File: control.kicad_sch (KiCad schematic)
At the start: 28 parts, among them J7 USB_C_Receptacle_USB2.0, J8 Conn_01x04_Male, J9 Conn_ARM_JTAG_SWD_10, U5 AMS1117-3.3, U6 STM32F042C4Tx

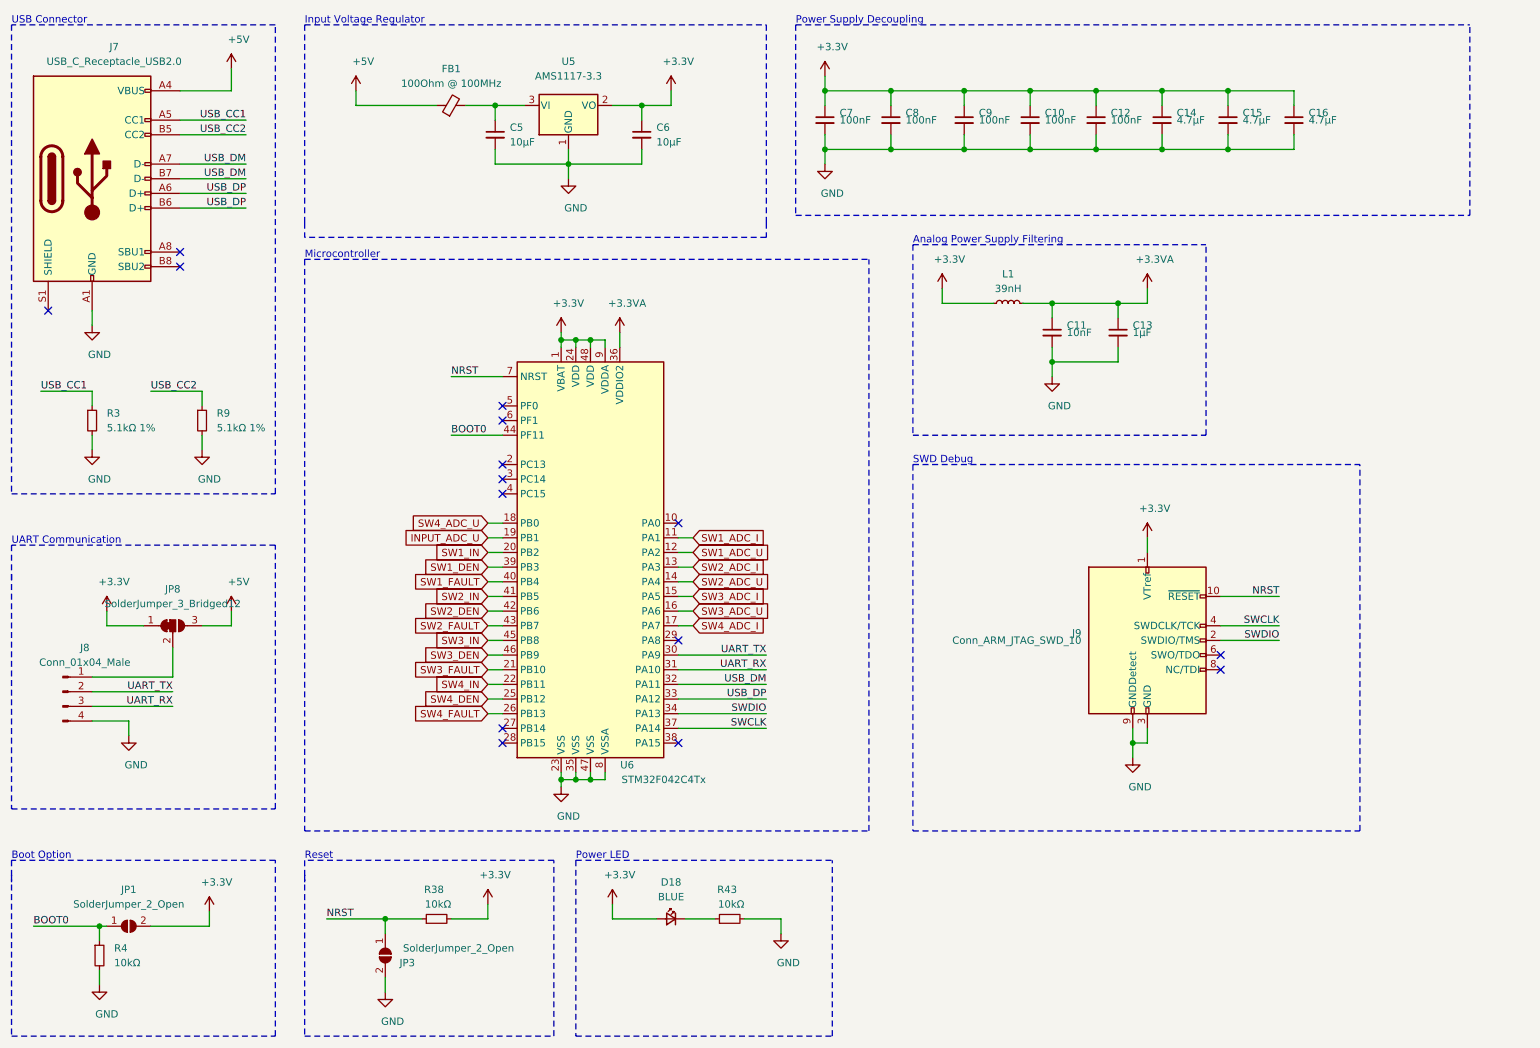
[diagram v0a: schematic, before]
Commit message: place decoupling capacitors nicer, add USB ESD protection
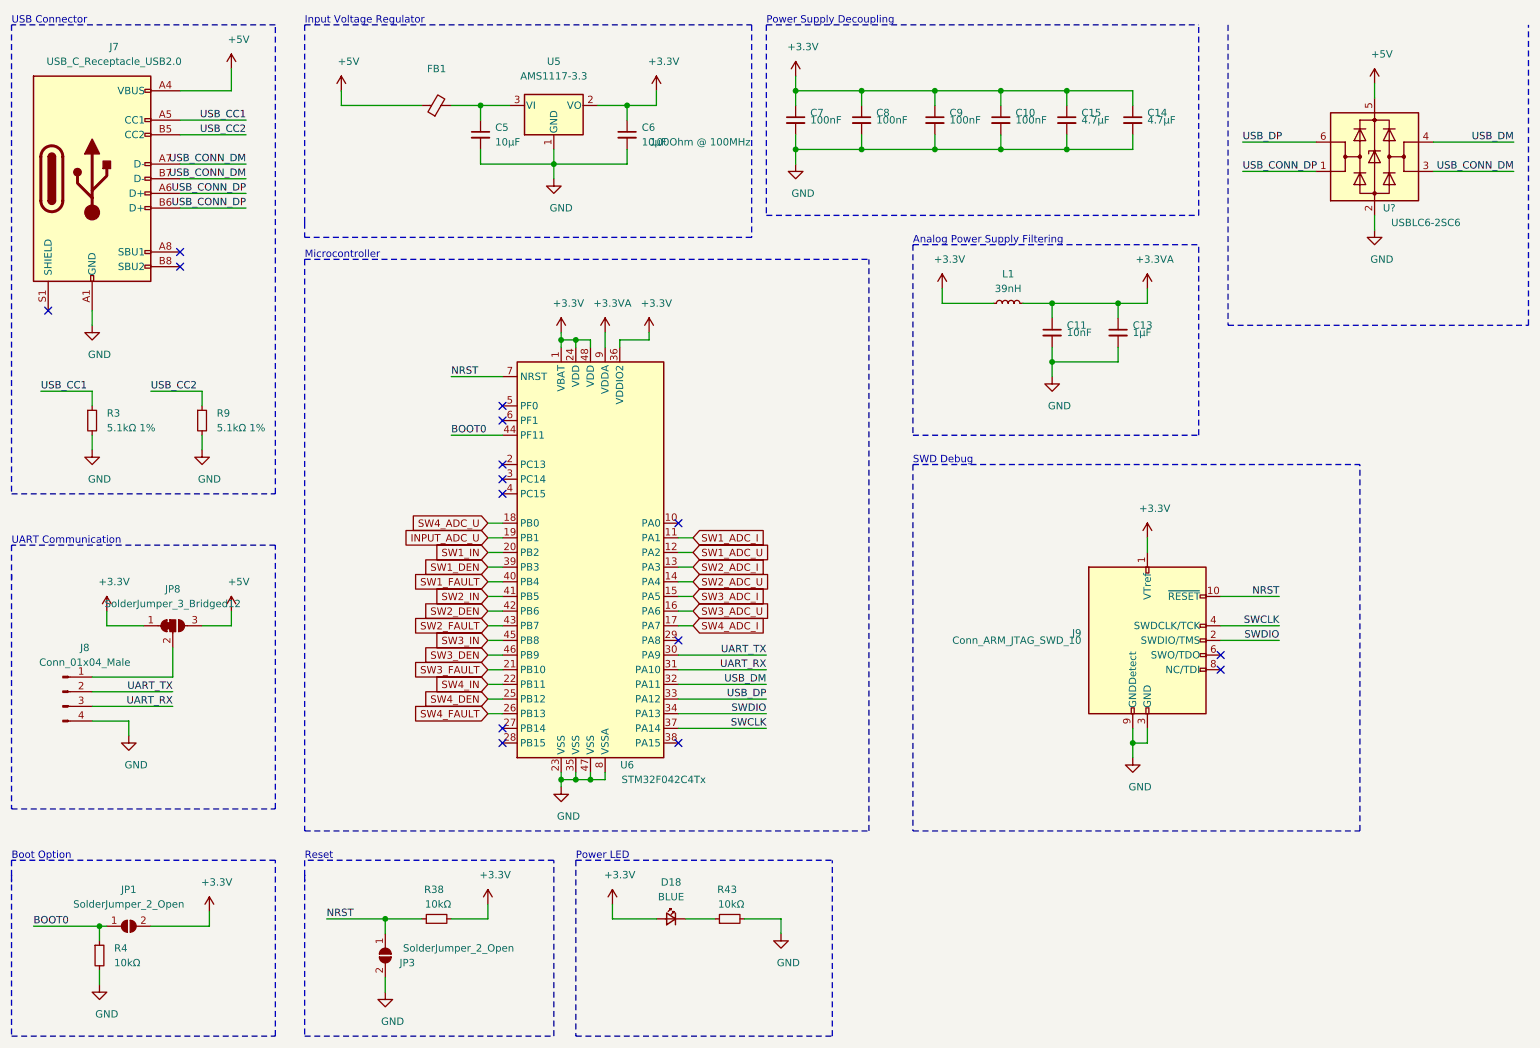
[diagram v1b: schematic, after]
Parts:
- removed C12: 100nF, Capacitor_SMD:C_0603_1608Metric, symbol Device:C_Small
- removed C15: 4.7µF, Capacitor_SMD:C_0603_1608Metric, symbol Device:C_Small
- added U?: USBLC6-2SC6, Package_TO_SOT_SMD:SOT-23-6, symbol Power_Protection:USBLC6-2SC6
- renumbered C16 to C15
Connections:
- net +3.3VA: now also U6.9 (VDDA); no longer U6.36 (VDDIO2)
- net +3V3: now also U6.36 (VDDIO2); no longer U6.9 (VDDA)
- net +5V: now also U?.5 (VBUS)
- net GND: now also U?.2 (GND)
- net USB_DM: now also U?.4 (I/O2); no longer J7.A7 (D-), J7.B7 (D-)
- net USB_DP: now also U?.6 (I/O1); no longer J7.A6 (D+), J7.B6 (D+)
- new net USB_CONN_DM: J7.A7 (D-), J7.B7 (D-), U?.3 (I/O2)
- new net USB_CONN_DP: J7.A6 (D+), J7.B6 (D+), U?.1 (I/O1)
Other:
- moved on the sheet: C10, C14, C15, C5, C6, C7, C8, C9, FB1, U5

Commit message: layouting finished, some microcontroller connection rearrangements
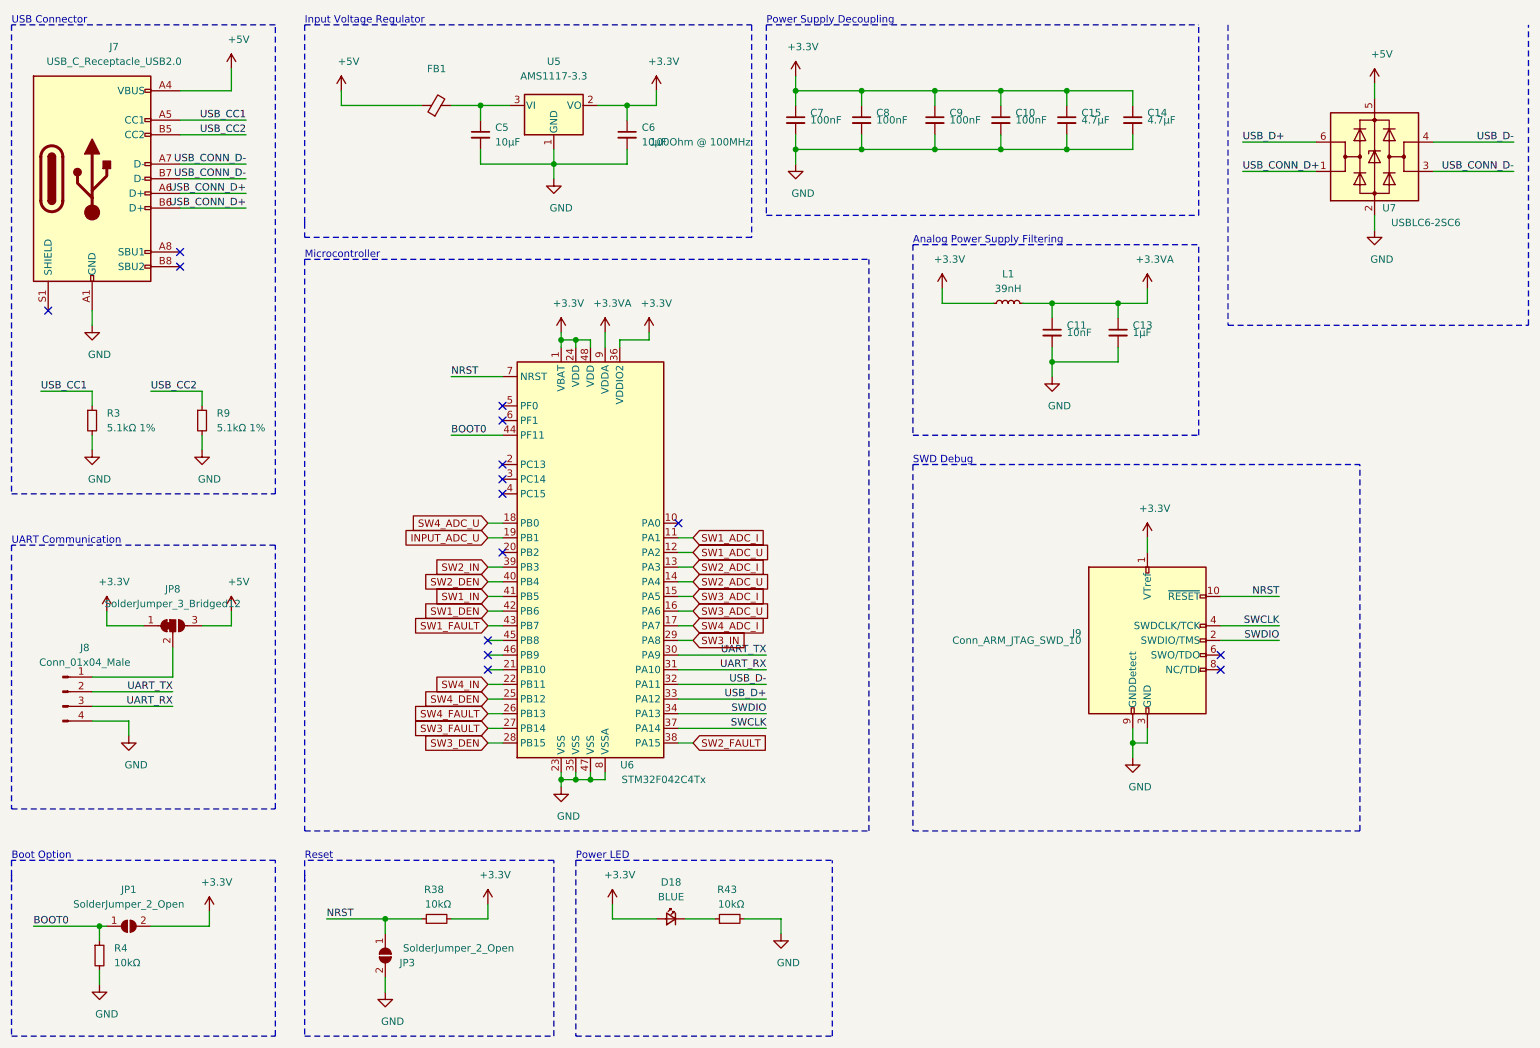
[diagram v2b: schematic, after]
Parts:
- gave numbers to parts that had none: 1
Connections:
- net SW1_DEN: now also U6.42 (PB6); no longer U6.39 (PB3)
- net SW1_FAULT: now also U6.43 (PB7); no longer U6.40 (PB4)
- net SW1_IN: now also U6.41 (PB5); no longer U6.20 (PB2)
- net SW2_DEN: now also U6.40 (PB4); no longer U6.42 (PB6)
- net SW2_FAULT: now also U6.38 (PA15); no longer U6.43 (PB7)
- net SW2_IN: now also U6.39 (PB3); no longer U6.41 (PB5)
- net SW3_DEN: now also U6.28 (PB15); no longer U6.46 (PB9)
- net SW3_FAULT: now also U6.27 (PB14); no longer U6.21 (PB10)
- net SW3_IN: now also U6.29 (PA8); no longer U6.45 (PB8)
- net USB_CONN_DM renamed USB_CONN_D-
- net USB_CONN_DP renamed USB_CONN_D+
- net USB_DM renamed USB_D-
- net USB_DP renamed USB_D+
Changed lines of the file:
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@@
   (junction (at 212.09 142.24) (diameter 1.016) (color 0 0 0 0))
   (no_connect (at 46.99 57.15))
+  (no_connect (at 100.33 124.46))
+  (no_connect (at 100.33 127))
+  (no_connect (at 100.33 129.54))
   (no_connect (at 46.99 59.69))
   (no_connect (at 227.33 129.54))
+  (no_connect (at 102.87 109.22))
   (no_connect (at 102.87 99.06))
   (no_connect (at 133.35 104.14))
-  (no_connect (at 102.87 142.24))
-  (no_connect (at 133.35 124.46))
-  (no_connect (at 133.35 142.24))
   (no_connect (at 102.87 93.98))
-  (no_connect (at 102.87 139.7))
   (no_connect (at 102.87 86.36))
   (no_connect (at 227.33 127))
@@
     (stroke (width 0) (type solid) (color 0 0 0 0))
   )
-  (wire (pts (xy 100.33 109.22) (xy 102.87 109.22))
-    (stroke (width 0) (type solid) (color 0 0 0 0))
-  )
   (wire (pts (xy 100.33 111.76) (xy 102.87 111.76))
     (stroke (width 0) (type solid) (color 0 0 0 0))
@@
     (stroke (width 0) (type solid) (color 0 0 0 0))
   )
+  (wire (pts (xy 100.33 139.7) (xy 102.87 139.7))
+    (stroke (width 0) (type solid) (color 0 0 0 0))
+  )
+  (wire (pts (xy 100.33 142.24) (xy 102.87 142.24))
+    (stroke (width 0) (type solid) (color 0 0 0 0))
+  )
   (wire (pts (xy 100.33 170.18) (xy 100.33 172.72))
     (stroke (width 0) (type solid) (color 0 0 0 0))
@@
     (stroke (width 0) (type solid) (color 0 0 0 0))
   )
+  (wire (pts (xy 133.35 124.46) (xy 135.89 124.46))
+    (stroke (width 0) (type solid) (color 0 0 0 0))
+  )
   (wire (pts (xy 133.35 127) (xy 148.59 127))
     (stroke (width 0) (type solid) (color 0 0 0 0))
@@
     (stroke (width 0) (type solid) (color 0 0 0 0))
   )
+  (wire (pts (xy 133.35 142.24) (xy 135.89 142.24))
+    (stroke (width 0) (type solid) (color 0 0 0 0))
+  )
   (wire (pts (xy 134.62 172.72) (xy 139.7 172.72))
     (stroke (width 0) (type solid) (color 0 0 0 0))
@@
     (effects (font (size 1.27 1.27)) (justify right bottom))
   )
-  (label "USB_CONN_DM" (at 58.42 41.91 180)
-    (effects (font (size 1.27 1.27)) (justify right bottom))
-  )
-  (label "USB_CONN_DM" (at 58.42 44.45 180)
-    (effects (font (size 1.27 1.27)) (justify right bottom))
-  )
-  (label "USB_CONN_DP" (at 58.42 46.99 180)
-    (effects (font (size 1.27 1.27)) (justify right bottom))
-  )
-  (label "USB_CONN_DP" (at 58.42 49.53 180)
+  (label "USB_CONN_D-" (at 58.42 41.91 180)
+    (effects (font (size 1.27 1.27)) (justify right bottom))
+  )
+  (label "USB_CONN_D-" (at 58.42 44.45 180)
+    (effects (font (size 1.27 1.27)) (justify right bottom))
+  )
+  (label "USB_CONN_D+" (at 58.42 46.99 180)
+    (effects (font (size 1.27 1.27)) (justify right bottom))
+  )
+  (label "USB_CONN_D+" (at 58.42 49.53 180)
     (effects (font (size 1.27 1.27)) (justify right bottom))
   )
@@
     (effects (font (size 1.27 1.27)) (justify right bottom))
   )
-  (label "USB_DM" (at 148.59 132.08 180)
-    (effects (font (size 1.27 1.27)) (justify right bottom))
-  )
-  (label "USB_DP" (at 148.59 134.62 180)
+  (label "USB_D-" (at 148.59 132.08 180)
+    (effects (font (size 1.27 1.27)) (justify right bottom))
+  )
+  (label "USB_D+" (at 148.59 134.62 180)
     (effects (font (size 1.27 1.27)) (justify right bottom))
   )
@@
     (effects (font (size 1.27 1.27)) (justify right bottom))
   )
-  (label "USB_DP" (at 231.14 38.1 0)
-    (effects (font (size 1.27 1.27)) (justify left bottom))
-  )
-  (label "USB_CONN_DP" (at 231.14 43.18 0)
+  (label "USB_D+" (at 231.14 38.1 0)
+    (effects (font (size 1.27 1.27)) (justify left bottom))
+  )
+  (label "USB_CONN_D+" (at 231.14 43.18 0)
     (effects (font (size 1.27 1.27)) (justify left bottom))
   )
@@
     (effects (font (size 1.27 1.27)) (justify right bottom))
   )
-  (label "USB_DM" (at 278.13 38.1 180)
-    (effects (font (size 1.27 1.27)) (justify right bottom))
-  )
-  (label "USB_CONN_DM" (at 278.13 43.18 180)
+  (label "USB_D-" (at 278.13 38.1 180)
+    (effects (font (size 1.27 1.27)) (justify right bottom))
+  )
+  (label "USB_CONN_D-" (at 278.13 43.18 180)
     (effects (font (size 1.27 1.27)) (justify right bottom))
   )
@@
     (effects (font (size 1.27 1.27)) (justify right))
   )
-  (global_label "SW1_IN" (shape input) (at 100.33 109.22 180)
+  (global_label "SW2_IN" (shape input) (at 100.33 111.76 180)
     (effects (font (size 1.27 1.27)) (justify right))
   )
-  (global_label "SW1_DEN" (shape input) (at 100.33 111.76 180)
+  (global_label "SW2_DEN" (shape input) (at 100.33 114.3 180)
     (effects (font (size 1.27 1.27)) (justify right))
   )
-  (global_label "SW1_FAULT" (shape input) (at 100.33 114.3 180)
+  (global_label "SW1_IN" (shape input) (at 100.33 116.84 180)
     (effects (font (size 1.27 1.27)) (justify right))
   )
-  (global_label "SW2_IN" (shape input) (at 100.33 116.84 180)
+  (global_label "SW1_DEN" (shape input) (at 100.33 119.38 180)
     (effects (font (size 1.27 1.27)) (justify right))
   )
-  (global_label "SW2_DEN" (shape input) (at 100.33 119.38 180)
-    (effects (font (size 1.27 1.27)) (justify right))
-  )
-  (global_label "SW2_FAULT" (shape input) (at 100.33 121.92 180)
-    (effects (font (size 1.27 1.27)) (justify right))
-  )
-  (global_label "SW3_IN" (shape input) (at 100.33 124.46 180)
-    (effects (font (size 1.27 1.27)) (justify right))
-  )
-  (global_label "SW3_DEN" (shape input) (at 100.33 127 180)
-    (effects (font (size 1.27 1.27)) (justify right))
-  )
-  (global_label "SW3_FAULT" (shape input) (at 100.33 129.54 180)
+  (global_label "SW1_FAULT" (shape input) (at 100.33 121.92 180)
     (effects (font (size 1.27 1.27)) (justify right))
   )
@@
     (effects (font (size 1.27 1.27)) (justify right))
   )
+  (global_label "SW3_FAULT" (shape input) (at 100.33 139.7 180)
+    (effects (font (size 1.27 1.27)) (justify right))
+  )
+  (global_label "SW3_DEN" (shape input) (at 100.33 142.24 180)
+    (effects (font (size 1.27 1.27)) (justify right))
+  )
   (global_label "SW1_ADC_I" (shape input) (at 135.89 106.68 0)
     (effects (font (size 1.27 1.27)) (justify left))
@@
   )
   (global_label "SW4_ADC_I" (shape input) (at 135.89 121.92 0)
+    (effects (font (size 1.27 1.27)) (justify left))
+  )
+  (global_label "SW3_IN" (shape input) (at 135.89 124.46 0)
+    (effects (font (size 1.27 1.27)) (justify left))
+  )
+  (global_label "SW2_FAULT" (shape input) (at 135.89 142.24 0)
     (effects (font (size 1.27 1.27)) (justify left))
   )
@@
   (symbol (lib_id "power:+5V") (at 254 27.94 0) (unit 1)
     (in_bom yes) (on_board yes)
-    (property "Reference" "#PWR?" (id 0) (at 254 31.75 0)
+    (property "Reference" "#PWR0101" (id 0) (at 254 31.75 0)
       (effects (font (size 1.27 1.27)) hide)
     )
@@
   (symbol (lib_id "power:GND") (at 254 53.34 0) (unit 1)
     (in_bom yes) (on_board yes)
-    (property "Reference" "#PWR?" (id 0) (at 254 59.69 0)
+    (property "Reference" "#PWR0102" (id 0) (at 254 59.69 0)
       (effects (font (size 1.27 1.27)) hide)
     )
@@
   (symbol (lib_id "Power_Protection:USBLC6-2SC6") (at 254 40.64 0) (unit 1)
     (in_bom yes) (on_board yes)
-    (property "Reference" "U?" (id 0) (at 256.54 49.53 0))
+    (property "Reference" "U7" (id 0) (at 256.54 49.53 0))
     (property "Value" "USBLC6-2SC6" (id 1) (at 262.89 52.07 0))
     (property "Footprint" "Package_TO_SOT_SMD:SOT-23-6" (id 2) (at 254 53.34 0)
